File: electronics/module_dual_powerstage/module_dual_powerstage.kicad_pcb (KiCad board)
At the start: 2 copper layers, 36.3 x 21.4 mm, 42 parts, among them J1 Conn_01x04, J2 Conn_01x04, Q1 60V4A, Q2 BC858B, Q3 BC847A, Q4 BC858B, Q5 BC847A, Q6 60V4A

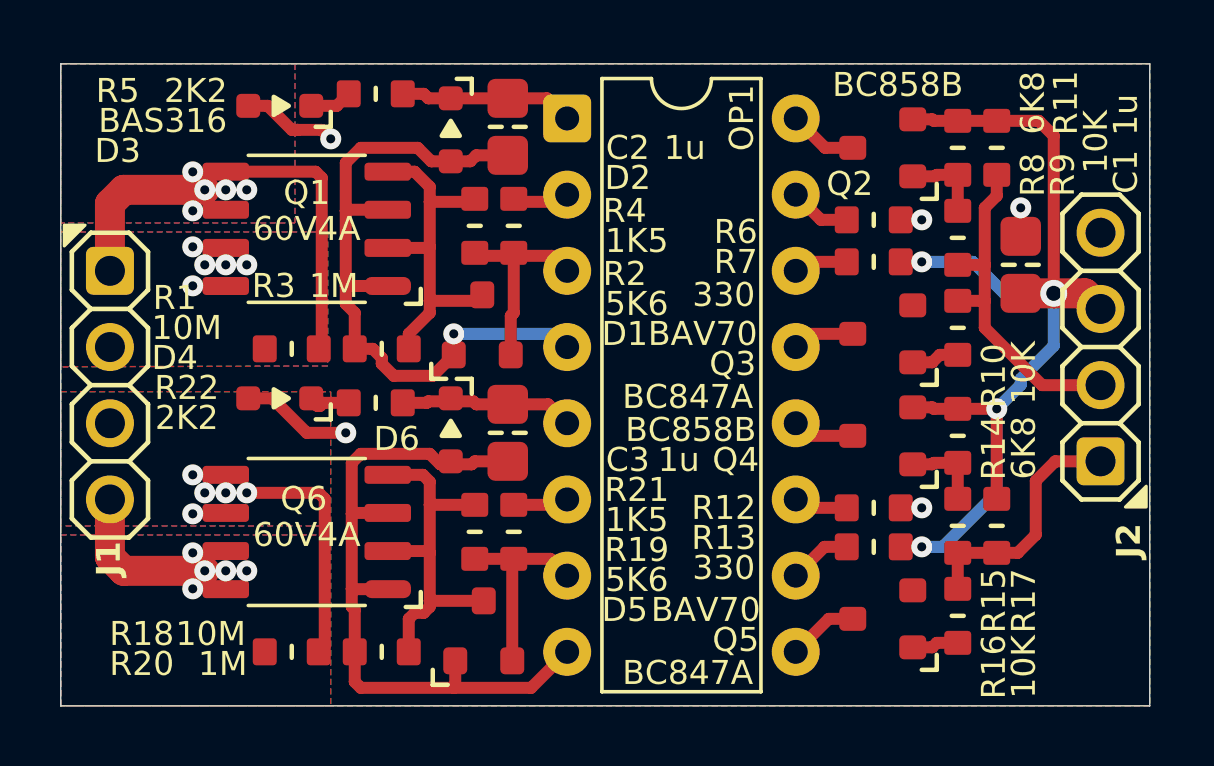
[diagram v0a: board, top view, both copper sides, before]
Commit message: ERC/DRC fixes, headers better aligned
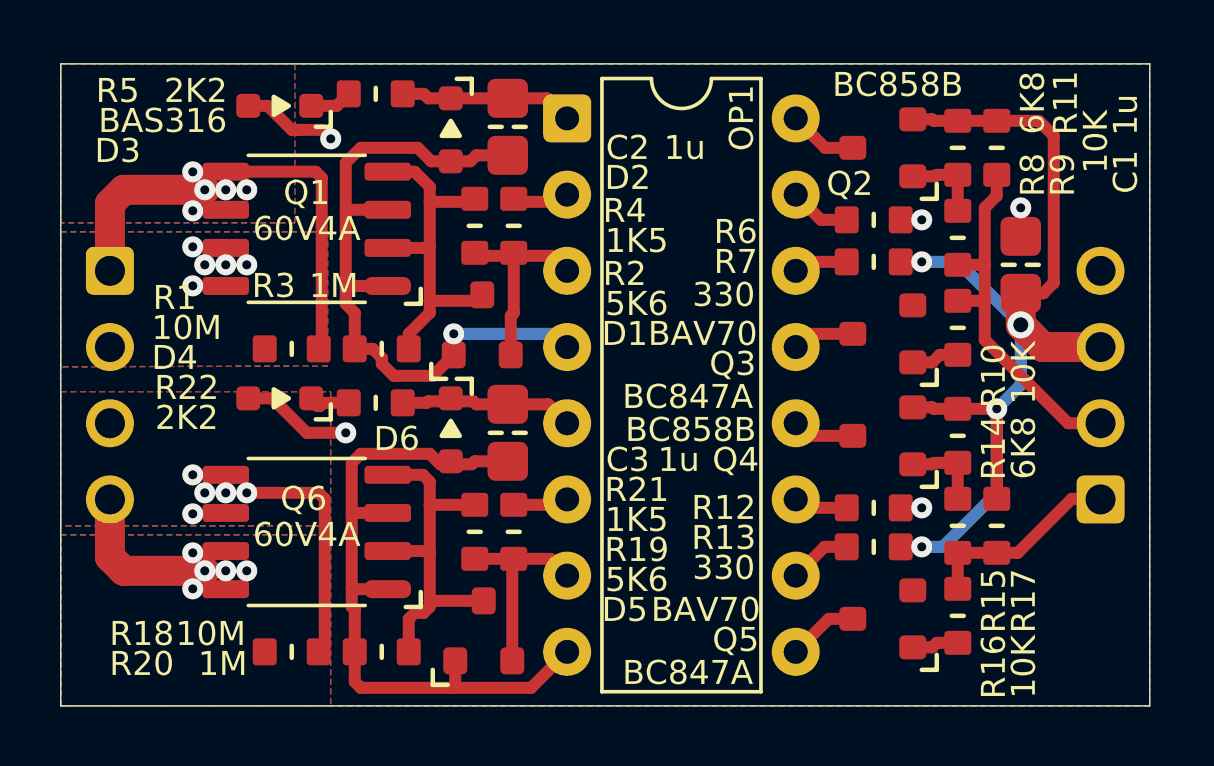
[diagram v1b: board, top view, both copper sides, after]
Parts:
- J1, J2: moved to B.Cu
- moved J2 1.27 mm to (188.0, 54.6)
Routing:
- net /SW2: track 8.28 -> 6.71 mm
- net /SW1: track 11.7 -> 12.5 mm

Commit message: preparation for production
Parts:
- N2: value 20250926 -> 20260118
- moved N1 9.28 mm to (183.0, 54.0)
- moved N2 9.28 mm to (183.0, 57.7)
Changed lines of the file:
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@@
 	(footprint "SquantorLabels:Label_Generic"
 		(layer "B.Cu")
-		(at 173.985 55.5 180)
+		(at 183 57.7 180)
 		(descr "Label for general purpose use")
 		(tags "Label")
@@
 			)
 		)
-		(property "Value" "20250926"
+		(property "Value" "20260118"
 			(at 0 0 0)
 			(layer "B.SilkS")
@@
 	(footprint "Symbol:OSHW-Symbol_6.7x6mm_SilkScreen"
 		(layer "B.Cu")
-		(at 173.985 51.8 180)
+		(at 183 54 180)
 		(descr "Open Source Hardware Symbol")
 		(tags "Logo Symbol OSHW")

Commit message: added tiled version
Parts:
- moved C1 124.1 mm to (62.0, 36.7)
- moved D2 124.1 mm to (43.0, 32.2)
- moved D5 124.1 mm to (44.1, 48.9)
- moved D6 124.1 mm to (43.0, 42.2)
- moved J2 124.1 mm to (64.7, 40.7)
- moved OP1 124.1 mm to (50.7, 40.7)
- moved R12 124.1 mm to (57.1, 44.8)
- moved R13 124.1 mm to (57.1, 46.1)
- moved R21 124.1 mm to (45.1, 45.6)
- moved R22 124.1 mm to (40.5, 41.3)
- moved R4 124.1 mm to (45.1, 35.4)
- moved R5 124.1 mm to (40.5, 31.0)
- moved R6 124.1 mm to (57.1, 35.2)
- moved R7 124.1 mm to (57.1, 36.6)
- moved D1 124.1 mm to (44.0, 38.7)
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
